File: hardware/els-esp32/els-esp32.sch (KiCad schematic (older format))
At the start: 32 parts, among them J1 USB B Micro, J5 Power, Q7 MMBT3904, Q8 MMBT3904, SW1 Reset, U1 AMS1117-3.3, U2 CP2104, U3 ESP32-WROOM-32

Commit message: minor layout
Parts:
- Q7, Q8: LCSC (none) -> C20526
- U1: LCSC (none) -> C6186
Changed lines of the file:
@@
 F 2 "Package_TO_SOT_SMD:SOT-223-3_TabPin2" H 1800 4050 50  0001 C CNN
 F 3 "http://www.advanced-monolithic.com/pdf/ds1117.pdf" H 1900 3600 50  0001 C CNN
+F 4 "C6186" H 1800 3850 50  0001 C CNN "LCSC"
 	1    1800 3850
 	1    0    0    -1
@@
 F 2 "Package_TO_SOT_SMD:SOT-23" H 4750 4075 50  0001 L CIN
 F 3 "https://www.onsemi.com/pub/Collateral/2N3903-D.PDF" H 4550 4150 50  0001 L CNN
+F 4 "C20526" H 4550 4150 50  0001 C CNN "LCSC"
 	1    4550 4150
 	1    0    0    -1
@@
 F 2 "Package_TO_SOT_SMD:SOT-23" H 4750 4775 50  0001 L CIN
 F 3 "https://www.onsemi.com/pub/Collateral/2N3903-D.PDF" H 4550 4850 50  0001 L CNN
+F 4 "C20526" H 4550 4850 50  0001 C CNN "LCSC"
 	1    4550 4850
 	1    0    0    -1

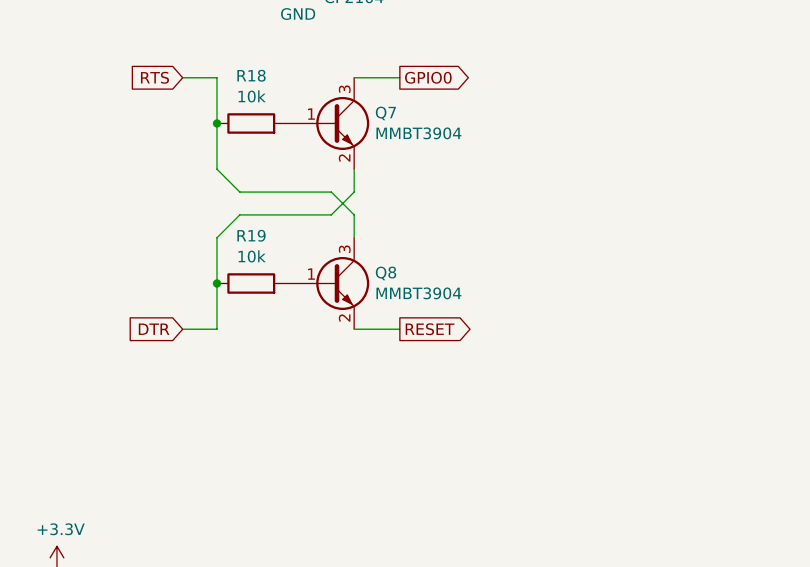
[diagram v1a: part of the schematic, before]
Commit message: Fixed hardware bug, one transistor was reversed
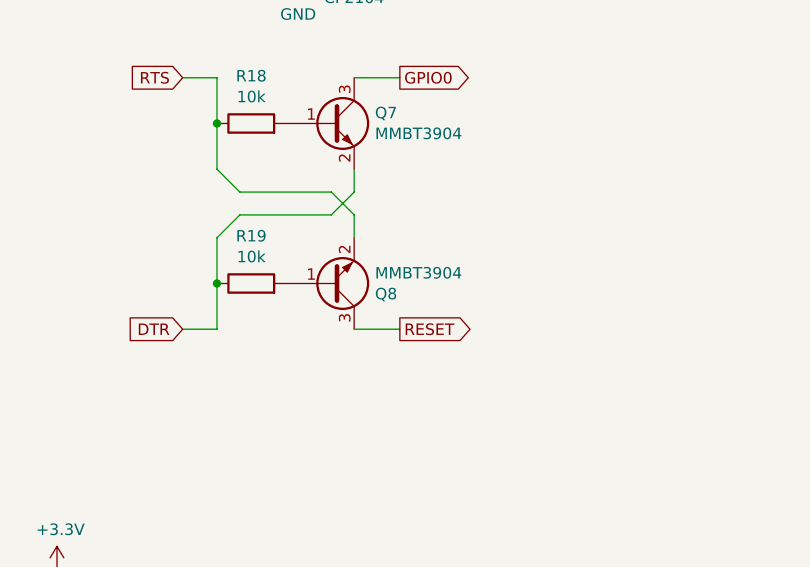
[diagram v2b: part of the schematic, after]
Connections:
- net RESET: now also Q8.3 (C); no longer Q8.2 (E)
- net RTS: now also Q8.2 (E); no longer Q8.3 (C)
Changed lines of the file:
@@
 F 4 "C20526" H 4550 4850 50  0001 C CNN "LCSC"
 	1    4550 4850
-	1    0    0    -1
+	1    0    0    1
 $EndComp
 $Comp
